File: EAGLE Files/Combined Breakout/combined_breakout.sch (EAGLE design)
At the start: 27 parts

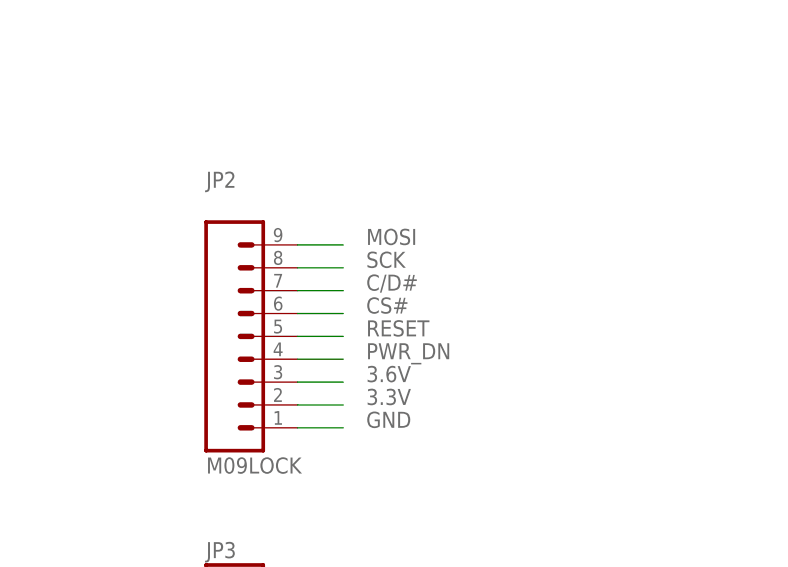
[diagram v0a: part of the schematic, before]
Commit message: Routing combined breakout board.
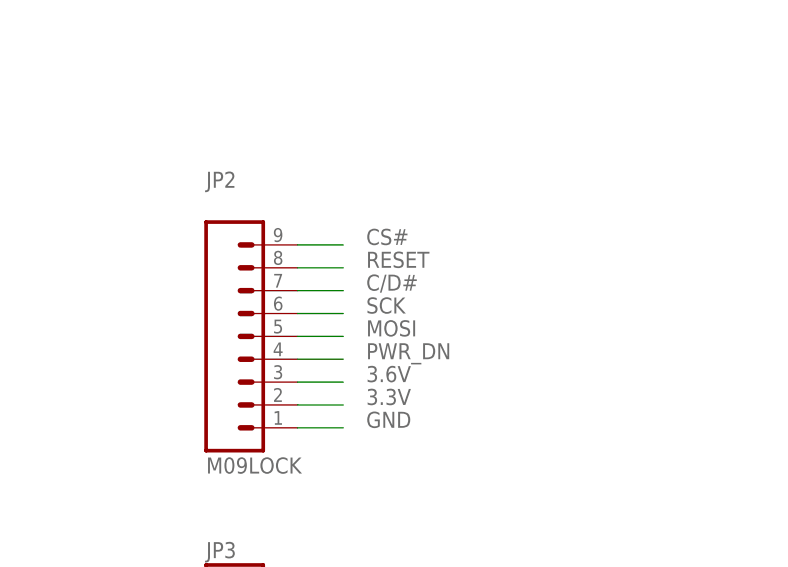
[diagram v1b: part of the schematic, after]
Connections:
- net CS#: now also JP2.9; no longer JP2.6
- net MOSI: now also JP2.5; no longer JP2.9
- net RESET: now also JP2.8; no longer JP2.5
- net SCK: now also JP2.6; no longer JP2.8
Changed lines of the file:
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@@
 </segment>
 <segment>
-<pinref part="JP2" gate="G$1" pin="6"/>
-<wire x1="149.86" y1="139.7" x2="154.94" y2="139.7" width="0.1524" layer="91"/>
-<label x="157.48" y="139.7" size="1.778" layer="95"/>
+<pinref part="JP2" gate="G$1" pin="9"/>
+<wire x1="149.86" y1="147.32" x2="154.94" y2="147.32" width="0.1524" layer="91"/>
+<label x="157.48" y="147.32" size="1.778" layer="95"/>
 </segment>
 </net>
@@
 </segment>
 <segment>
-<pinref part="JP2" gate="G$1" pin="5"/>
-<wire x1="149.86" y1="137.16" x2="154.94" y2="137.16" width="0.1524" layer="91"/>
-<label x="157.48" y="137.16" size="1.778" layer="95"/>
+<pinref part="JP2" gate="G$1" pin="8"/>
+<wire x1="149.86" y1="144.78" x2="154.94" y2="144.78" width="0.1524" layer="91"/>
+<label x="157.48" y="144.78" size="1.778" layer="95"/>
 </segment>
 </net>
@@
 </segment>
 <segment>
-<pinref part="JP2" gate="G$1" pin="8"/>
-<wire x1="149.86" y1="144.78" x2="154.94" y2="144.78" width="0.1524" layer="91"/>
-<label x="157.48" y="144.78" size="1.778" layer="95"/>
+<pinref part="JP2" gate="G$1" pin="6"/>
+<wire x1="149.86" y1="139.7" x2="154.94" y2="139.7" width="0.1524" layer="91"/>
+<label x="157.48" y="139.7" size="1.778" layer="95"/>
 </segment>
 </net>
@@
 </segment>
 <segment>
-<pinref part="JP2" gate="G$1" pin="9"/>
-<wire x1="149.86" y1="147.32" x2="154.94" y2="147.32" width="0.1524" layer="91"/>
-<label x="157.48" y="147.32" size="1.778" layer="95"/>
+<pinref part="JP2" gate="G$1" pin="5"/>
+<wire x1="149.86" y1="137.16" x2="154.94" y2="137.16" width="0.1524" layer="91"/>
+<label x="157.48" y="137.16" size="1.778" layer="95"/>
 </segment>
 </net>

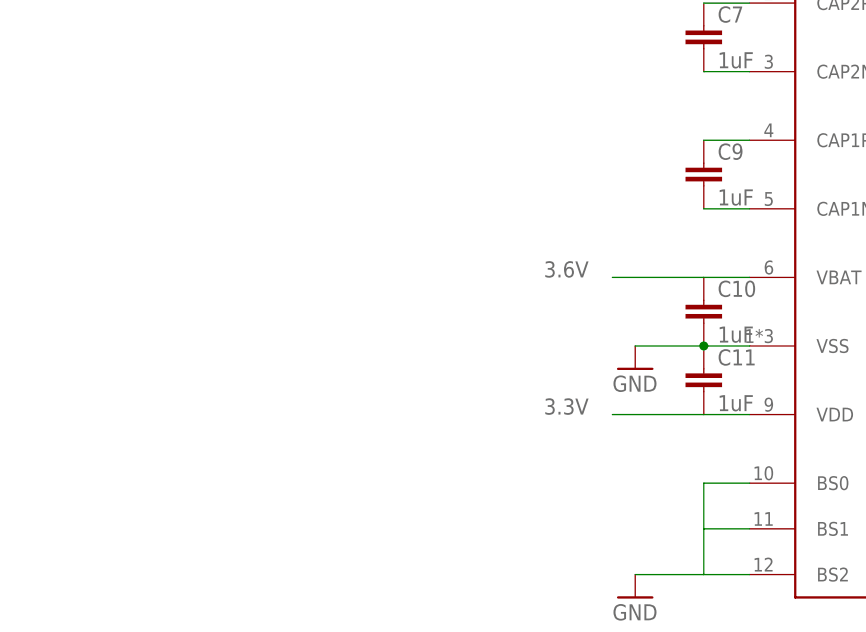
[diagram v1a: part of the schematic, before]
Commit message: Finally finished combined breakout board. It's pretty ugly but it will work for prototyping purposes.
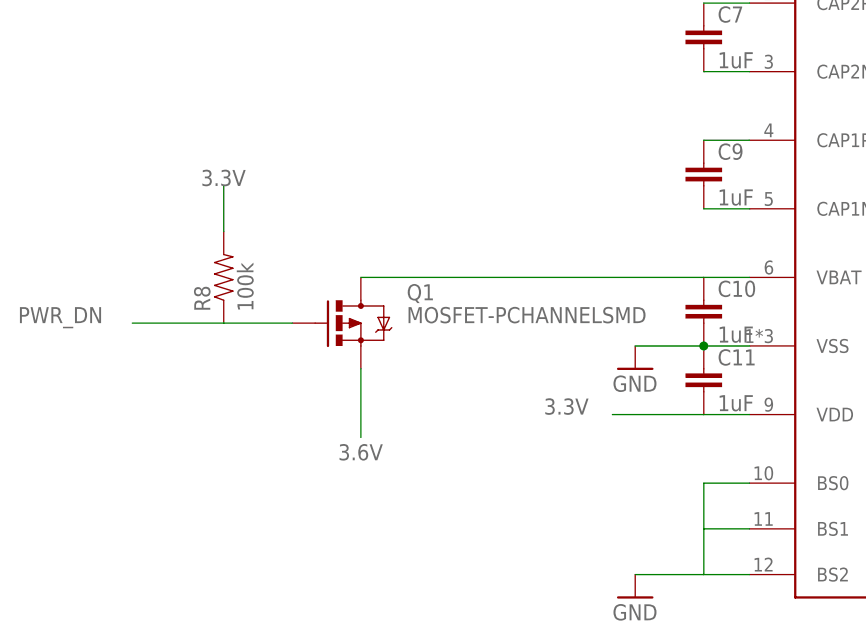
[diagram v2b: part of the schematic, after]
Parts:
- added Q1: MOSFET-PCHANNELSMD, chips:MOSFET-PCHANNELSMD
- added R8: 100k, chips:RESISTOR0402-S
- C10, C11, C12, C13, C7, C9: device chips:CAP0402-CAP -> chips:CAP0402-S
- R7: device chips:RESISTOR0402-RES -> chips:RESISTOR0402-S
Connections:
- new net N$15: C10.1, Q1.D, U$3.VBAT
- net 3.3V: now also R8.2
- net 3.6V: now also Q1.S; no longer C10.1, U$3.VBAT
- net PWR_DN: now also Q1.G, R8.1
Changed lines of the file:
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@@
 <part name="GND3" library="supply1" deviceset="GND" device=""/>
 <part name="GND4" library="supply1" deviceset="GND" device=""/>
-<part name="C7" library="chips" deviceset="CAP" device="0402-CAP" value="1uF"/>
-<part name="C9" library="chips" deviceset="CAP" device="0402-CAP" value="1uF"/>
-<part name="C10" library="chips" deviceset="CAP" device="0402-CAP" value="1uF"/>
-<part name="C11" library="chips" deviceset="CAP" device="0402-CAP" value="1uF"/>
-<part name="C12" library="chips" deviceset="CAP" device="0402-CAP" value="2.2uF"/>
-<part name="C13" library="chips" deviceset="CAP" device="0402-CAP" value="4.7uF"/>
-<part name="R7" library="chips" deviceset="RESISTOR" device="0402-RES" value="390K"/>
+<part name="C7" library="chips" deviceset="CAP" device="0402-S" value="1uF"/>
+<part name="C9" library="chips" deviceset="CAP" device="0402-S" value="1uF"/>
+<part name="C10" library="chips" deviceset="CAP" device="0402-S" value="1uF"/>
+<part name="C11" library="chips" deviceset="CAP" device="0402-S" value="1uF"/>
+<part name="C12" library="chips" deviceset="CAP" device="0402-S" value="2.2uF"/>
+<part name="C13" library="chips" deviceset="CAP" device="0402-S" value="4.7uF"/>
+<part name="R7" library="chips" deviceset="RESISTOR" device="0402-S" value="390K"/>
 <part name="GND5" library="supply1" deviceset="GND" device=""/>
 <part name="GND6" library="supply1" deviceset="GND" device=""/>
@@
 <part name="JP2" library="SparkFun-Connectors" deviceset="M09" device="LOCK"/>
 <part name="JP3" library="SparkFun-Connectors" deviceset="M02" device="LOCK"/>
+<part name="Q1" library="chips" deviceset="MOSFET-PCHANNEL" device="SMD"/>
+<part name="R8" library="chips" deviceset="RESISTOR" device="0402-S" value="100k"/>
 </parts>
 <sheets>
@@
 <instance part="JP2" gate="G$1" x="139.7" y="137.16"/>
 <instance part="JP3" gate="G$1" x="142.24" y="106.68"/>
+<instance part="Q1" gate="G$1" x="-2.54" y="132.08"/>
+<instance part="R8" gate="G$1" x="-17.78" y="137.16" rot="R90"/>
 </instances>
 <busses>
@@
 </segment>
 <segment>
-<pinref part="U$3" gate="G$1" pin="VBAT"/>
-<pinref part="C10" gate="G$1" pin="1"/>
-<wire x1="40.64" y1="137.16" x2="35.56" y2="137.16" width="0.1524" layer="91"/>
-<wire x1="35.56" y1="137.16" x2="25.4" y2="137.16" width="0.1524" layer="91"/>
-<label x="17.78" y="137.16" size="1.778" layer="95"/>
-</segment>
-<segment>
 <pinref part="JP2" gate="G$1" pin="3"/>
 <wire x1="149.86" y1="132.08" x2="154.94" y2="132.08" width="0.1524" layer="91"/>
 <label x="157.48" y="132.08" size="1.778" layer="95"/>
+</segment>
+<segment>
+<pinref part="Q1" gate="G$1" pin="S"/>
+<wire x1="-2.54" y1="127" x2="-2.54" y2="119.38" width="0.1524" layer="91"/>
+<label x="-5.08" y="116.84" size="1.778" layer="95"/>
 </segment>
 </net>
@@
 <label x="157.48" y="129.54" size="1.778" layer="95"/>
 </segment>
+<segment>
+<pinref part="R8" gate="G$1" pin="2"/>
+<wire x1="-17.78" y1="142.24" x2="-17.78" y2="147.32" width="0.1524" layer="91"/>
+<label x="-20.32" y="147.32" size="1.778" layer="95"/>
+</segment>
 </net>
 <net name="N$1" class="0">
@@
 <label x="157.48" y="134.62" size="1.778" layer="95"/>
 </segment>
-</net>
+<segment>
+<pinref part="Q1" gate="G$1" pin="G"/>
+<pinref part="R8" gate="G$1" pin="1"/>
+<wire x1="-10.16" y1="132.08" x2="-17.78" y2="132.08" width="0.1524" layer="91"/>
+<wire x1="-17.78" y1="132.08" x2="-27.94" y2="132.08" width="0.1524" layer="91"/>
+<label x="-40.64" y="132.08" size="1.778" layer="95"/>
+</segment>
+</net>
+<net name="N$15" class="0">
+<segment>
+<pinref part="U$3" gate="G$1" pin="VBAT"/>
+<pinref part="C10" gate="G$1" pin="1"/>
+<wire x1="40.64" y1="137.16" x2="35.56" y2="137.16" width="0.1524" layer="91"/>
+<pinref part="Q1" gate="G$1" pin="D"/>
+<wire x1="-2.54" y1="137.16" x2="35.56" y2="137.16" width="0.1524" layer="91"/>
+</segment>
+</net>

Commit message: Adjusted spacing on some of the components on the combined breakout board. Removed some silkscreen that was in the way. Checked with freeDFM, sent gerbers off to circuitgraphics!
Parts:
- U$1: device brent:LM3990 -> intelliDesk:LM3990
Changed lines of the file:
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@@
 </classes>
 <parts>
-<part name="U$1" library="brent" deviceset="LM3990" device=""/>
+<part name="U$1" library="intelliDesk" deviceset="LM3990" device=""/>
 <part name="L1" library="brent" deviceset="NR6028T150M" device="" value="15uH"/>
 <part name="C1" library="chips" deviceset="CAP" device="0603-CAP" value="100nF"/>
